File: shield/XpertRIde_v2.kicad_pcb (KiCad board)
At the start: 2 copper layers, 55.3 x 50.5 mm, 44 parts, among them J1 Conn_01x20, J2 USB_B_Micro, J3 Conn_02x05_Counter_Clockwise, J4 Conn_01x01_Female, J5 Conn_01x01_Female, J6 Conn_01x01_Female, J7 Conn_01x05, SW1 SW_DPDT_x2, U1 MCP6N11-001, U2 ADG728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

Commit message: new design
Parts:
- J7: value Conn_01x05 -> Conn_02x10_Odd_Even; footprint Connector_FFC-FPC:TE_84952-5_1x05-1MP_P1.0mm_Horizontal -> Pin_Headers:Pin_Header_Straight_2x10_Pitch2.54mm
- moved J7 34.4 mm to (68.9, 103.0), turned to 270 degrees
- moved R18 12.4 mm to (71.9, 82.3)
- moved U5 12.4 mm to (78.0, 75.6)
- moved C1 12.4 mm to (64.8, 80.7)
- moved C2 12.4 mm to (59.8, 93.7)
- moved C4 12.4 mm to (77.8, 80.6)
- moved C5 12.4 mm to (81.0, 75.6)
- moved R1 12.4 mm to (58.2, 81.4)
- moved R10 12.4 mm to (84.1, 94.2)
- moved R11 12.4 mm to (84.1, 92.7)
- moved R12 12.4 mm to (84.1, 91.2)
- moved R13 12.4 mm to (81.1, 80.6)
- moved R14 12.4 mm to (84.4, 86.4)
- moved R16 12.4 mm to (84.4, 83.6)
- moved R17 12.4 mm to (84.4, 82.2)
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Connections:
- J7 pad 1: /AMP_OUT -> /TWI_CLK
- J7 pad 2: /TWI_CLK -> /TWI_SDA
- J7 pad 3: /TWI_SDA -> /AMP_OUT
- J7 pad 4: VDD -> (no net)
- J7 pad 5: GNDD -> (no net)
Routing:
- net VDD: track 186.7 -> 149.1 mm, vias 15 -> 12
- net /AMP_OUT: track 70.2 -> 42.4 mm, vias 5 -> 4
- net /Sensor8: track 10.6 -> 28.2 mm
- net /Sensor7: track 12.1 -> 28.7 mm
- net /Sensor6: track 13.9 -> 29.2 mm
- net /Sensor3: track 13.9 -> 27.8 mm
- net /Sensor5: track 16.3 -> 29.8 mm
- net /Sensor2: track 12.7 -> 25.3 mm
- net /Sensor1: track 13.2 -> 25.7 mm
- net /Sensor4: track 14.5 -> 26.8 mm
- net GNDD: track 67.4 -> 56.7 mm, vias 32 -> 47
- net /TWI_SDA: track 81.6 -> 90.8 mm, vias 5 -> 7
- net /TWI_CLK: track 86.9 -> 80.6 mm, vias 6 -> 3
- net Net-(R5-Pad1): track 9.64 -> 11.8 mm

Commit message: MOdif_size
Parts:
- moved G*** 3.83 mm to (62.6, 69.1)
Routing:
- net Net-(J6-Pad1): vias 0 -> 2
- net VDD: vias 12 -> 13
- net GNDD: vias 47 -> 99
- net /TWI_CLK: vias 3 -> 4
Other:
- board size 55.3 x 50.5 mm -> 59.6 x 59.6 mm

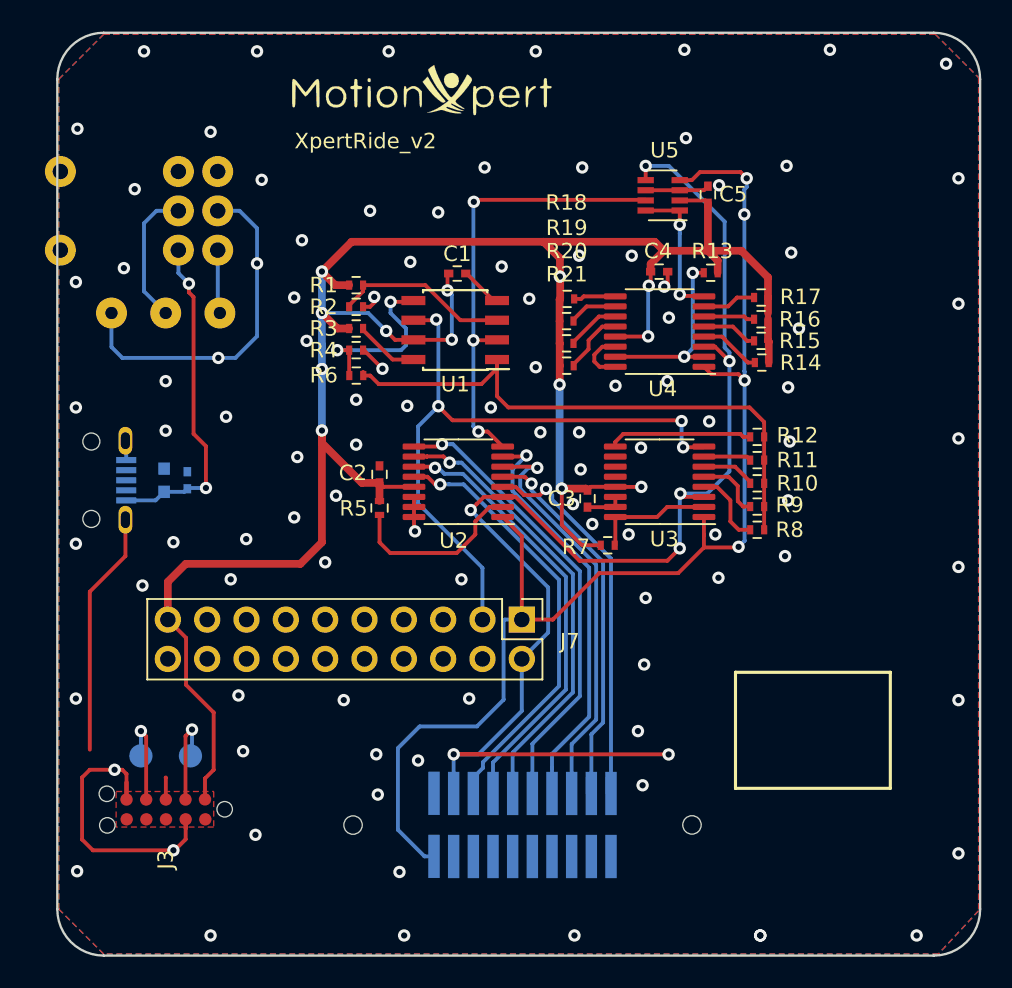
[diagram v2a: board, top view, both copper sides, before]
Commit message: new PCB dimensions
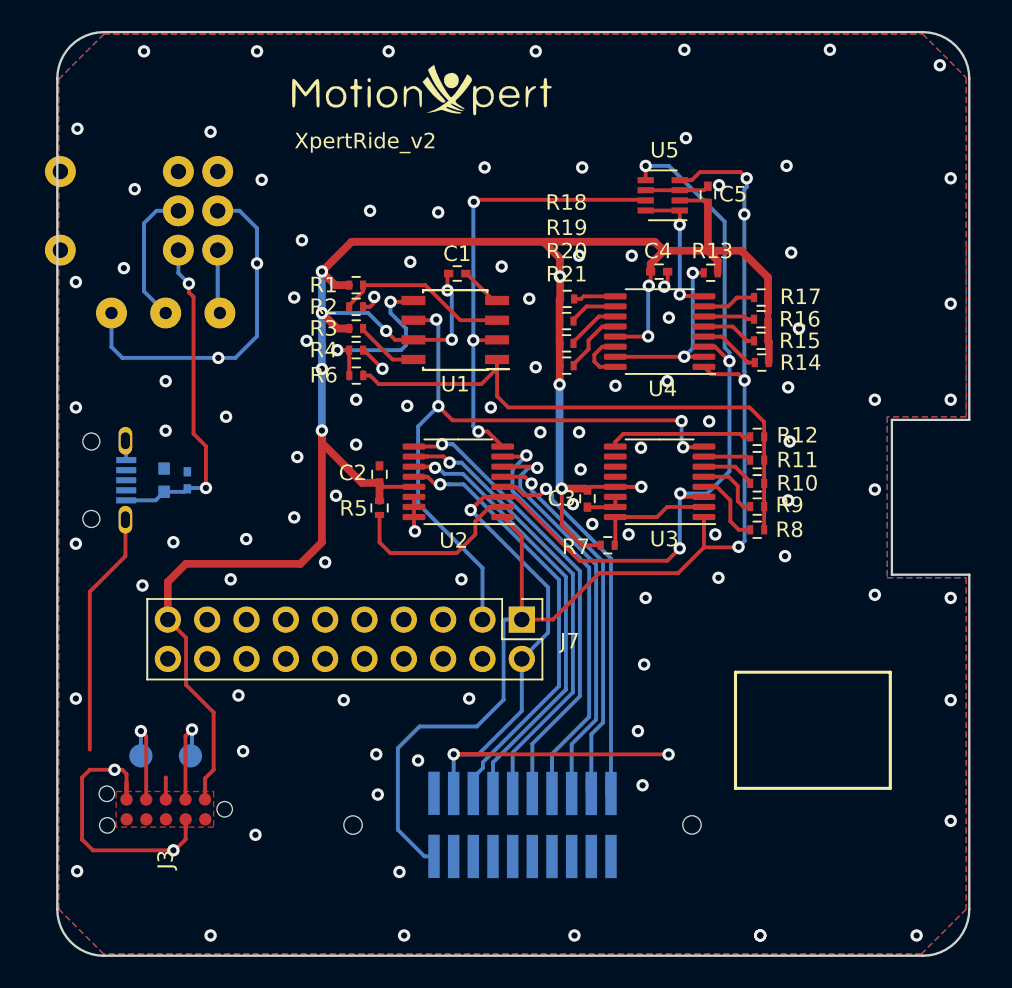
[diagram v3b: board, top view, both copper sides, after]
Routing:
- net GNDD: vias 99 -> 102
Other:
- board size 59.6 x 59.6 mm -> 58.9 x 59.7 mm
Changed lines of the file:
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@@
   (general
     (thickness 1.6)
-    (drawings 13)
-    (tracks 604)
+    (drawings 17)
+    (tracks 607)
     (zones 0)
     (modules 44)
@@
     (mod_text_size 1 1)
     (mod_text_width 0.15)
-    (pad_size 1.524 1.524)
-    (pad_drill 0.762)
+    (pad_size 2 2)
+    (pad_drill 1)
     (pad_to_mask_clearance 0.051)
     (solder_mask_min_width 0.25)
@@
     (fp_line (start 4 0) (end -4 0) (layer B.SilkS) (width 0.15))
     (fp_line (start -4 7.6) (end 4 7.6) (layer B.SilkS) (width 0.15))
-    (pad "" thru_hole circle (at 2.54 0 90) (size 2 2) (drill 1) (layers *.Cu *.Mask))
-    (pad "" thru_hole circle (at -2.54 0 90) (size 2 2) (drill 1) (layers *.Cu *.Mask))
+    (pad "" np_thru_hole circle (at 2.54 0 90) (size 2 2) (drill 1) (layers *.Cu *.Mask))
+    (pad "" np_thru_hole circle (at -2.54 0 90) (size 2 2) (drill 1) (layers *.Cu *.Mask))
     (pad 6 thru_hole circle (at -2.54 10.16 90) (size 2 2) (drill 1) (layers *.Cu *.Mask)
       (net 16 "Net-(J4-Pad1)"))
@@
     )
   )
-  (gr_arc (start 41.94 121.74) (end 38.94 121.74) (angle -90) (layer Edge.Cuts) (width 0.15))
-  (gr_arc (start 95.54 121.74) (end 95.54 124.74) (angle -90) (layer Edge.Cuts) (width 0.15))
-  (gr_arc (start 95.54 68.14) (end 98.54 68.14) (angle -90) (layer Edge.Cuts) (width 0.15))
-  (gr_arc (start 41.94 68.14) (end 41.94 65.14) (angle -90) (layer Edge.Cuts) (width 0.15))
-  (gr_line (start 98.54 68.14) (end 98.54 121.74) (layer Edge.Cuts) (width 0.15))
-  (gr_line (start 38.94 121.74) (end 38.94 68.14) (layer Edge.Cuts) (width 0.15))
-  (gr_line (start 95.54 124.74) (end 41.94 124.74) (layer Edge.Cuts) (width 0.15))
-  (gr_line (start 41.94 65.14) (end 95.54 65.14) (layer Edge.Cuts) (width 0.15))
+  (gr_line (start 97.84 100.14) (end 97.84 121.75) (layer Edge.Cuts) (width 0.15))
+  (gr_line (start 97.84 68.1) (end 97.84 90.14) (layer Edge.Cuts) (width 0.15))
+  (gr_line (start 92.84 100.14) (end 97.84 100.14) (layer Edge.Cuts) (width 0.15))
+  (gr_line (start 92.84 90.14) (end 92.84 100.14) (layer Edge.Cuts) (width 0.15))
+  (gr_line (start 97.84 90.14) (end 92.84 90.14) (layer Edge.Cuts) (width 0.15))
+  (gr_arc (start 41.94 121.75) (end 38.94 121.75) (angle -90) (layer Edge.Cuts) (width 0.15))
+  (gr_arc (start 94.84 121.75) (end 94.84 124.75) (angle -90) (layer Edge.Cuts) (width 0.15))
+  (gr_arc (start 94.84 68.1) (end 97.84 68.1) (angle -90) (layer Edge.Cuts) (width 0.15))
+  (gr_arc (start 41.94 68.1) (end 41.94 65.1) (angle -90) (layer Edge.Cuts) (width 0.15))
+  (gr_line (start 38.94 121.75) (end 38.94 68.1) (layer Edge.Cuts) (width 0.15))
+  (gr_line (start 94.84 124.75) (end 41.94 124.75) (layer Edge.Cuts) (width 0.15))
+  (gr_line (start 41.94 65.1) (end 94.84 65.1) (layer Edge.Cuts) (width 0.15))
   (gr_text XpertRide_v2 (at 58.84 72.14) (layer F.SilkS)
     (effects (font (size 1 1) (thickness 0.15)))
@@
   (via (at 78.44 83.54) (size 0.8) (drill 0.4) (layers F.Cu B.Cu) (net 2))
   (via (at 88.84 66.24) (size 0.8) (drill 0.4) (layers F.Cu B.Cu) (net 2))
-  (via (at 96.34 67.14) (size 0.8) (drill 0.4) (layers F.Cu B.Cu) (net 2))
-  (via (at 97.14 74.54) (size 0.8) (drill 0.4) (layers F.Cu B.Cu) (net 2))
-  (via (at 97.14 82.64) (size 0.8) (drill 0.4) (layers F.Cu B.Cu) (net 2))
-  (via (at 97.14 91.34) (size 0.8) (drill 0.4) (layers F.Cu B.Cu) (net 2))
-  (via (at 97.14 99.64) (size 0.8) (drill 0.4) (layers F.Cu B.Cu) (net 2))
-  (via (at 97.14 108.24) (size 0.8) (drill 0.4) (layers F.Cu B.Cu) (net 2))
-  (via (at 97.14 118.14) (size 0.8) (drill 0.4) (layers F.Cu B.Cu) (net 2))
+  (via (at 95.94 67.24) (size 0.8) (drill 0.4) (layers F.Cu B.Cu) (net 2))
+  (via (at 96.64 74.54) (size 0.8) (drill 0.4) (layers F.Cu B.Cu) (net 2))
+  (via (at 96.64 82.64) (size 0.8) (drill 0.4) (layers F.Cu B.Cu) (net 2))
+  (via (at 96.64 108.24) (size 0.8) (drill 0.4) (layers F.Cu B.Cu) (net 2))
+  (via (at 96.64 116.04) (size 0.8) (drill 0.4) (layers F.Cu B.Cu) (net 2))
   (via (at 94.44 123.44) (size 0.8) (drill 0.4) (layers F.Cu B.Cu) (net 2))
   (via (at 84.34 123.44) (size 0.8) (drill 0.4) (layers F.Cu B.Cu) (net 2))
@@
   (via (at 59.64 114.34) (size 0.8) (drill 0.4) (layers F.Cu B.Cu) (net 2))
   (via (at 61.04 119.34) (size 0.8) (drill 0.4) (layers F.Cu B.Cu) (net 2))
+  (via (at 96.64 88.84) (size 0.8) (drill 0.4) (layers F.Cu B.Cu) (net 2))
+  (via (at 91.74 88.84) (size 0.8) (drill 0.4) (layers F.Cu B.Cu) (net 2))
+  (via (at 91.74 94.64) (size 0.8) (drill 0.4) (layers F.Cu B.Cu) (net 2))
+  (via (at 91.74 101.44) (size 0.8) (drill 0.4) (layers F.Cu B.Cu) (net 2))
+  (via (at 96.64 101.64) (size 0.8) (drill 0.4) (layers F.Cu B.Cu) (net 2))
   (segment (start 47.14 94.79) (end 47.34 94.59) (width 0.25) (layer B.Cu) (net 3) (status 30))
   (segment (start 45.84 94.79) (end 47.14 94.79) (width 0.25) (layer B.Cu) (net 3) (status 30))
@@
     (polygon
       (pts
-        (xy 39.04 68.14) (xy 41.94 65.24) (xy 95.64 65.24) (xy 98.44 68.04) (xy 98.44 121.84)
-        (xy 95.84 124.64) (xy 41.94 124.64) (xy 39.04 121.74)
+        (xy 39.04 68.14) (xy 41.94 65.24) (xy 94.84 65.24) (xy 97.64 68.04) (xy 97.64 89.94)
+        (xy 92.54 89.94) (xy 92.54 100.34) (xy 97.64 100.34) (xy 97.64 121.74) (xy 94.74 124.64)
+        (xy 41.94 124.64) (xy 39.04 121.74)
       )
     )
@@
     (polygon
       (pts
-        (xy 39.04 68.14) (xy 41.94 65.24) (xy 95.64 65.24) (xy 98.44 68.04) (xy 98.44 121.84)
-        (xy 95.84 124.64) (xy 41.94 124.64) (xy 39.04 121.74)
+        (xy 39.04 68.14) (xy 41.94 65.24) (xy 94.84 65.24) (xy 97.64 68.04) (xy 97.64 78.99)
+        (xy 97.64 89.94) (xy 92.54 89.94) (xy 92.54 100.34) (xy 97.64 100.34) (xy 97.64 121.74)
+        (xy 94.74 124.64) (xy 41.94 124.64) (xy 39.04 121.74)
       )
     )

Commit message: modif dimensions-joint
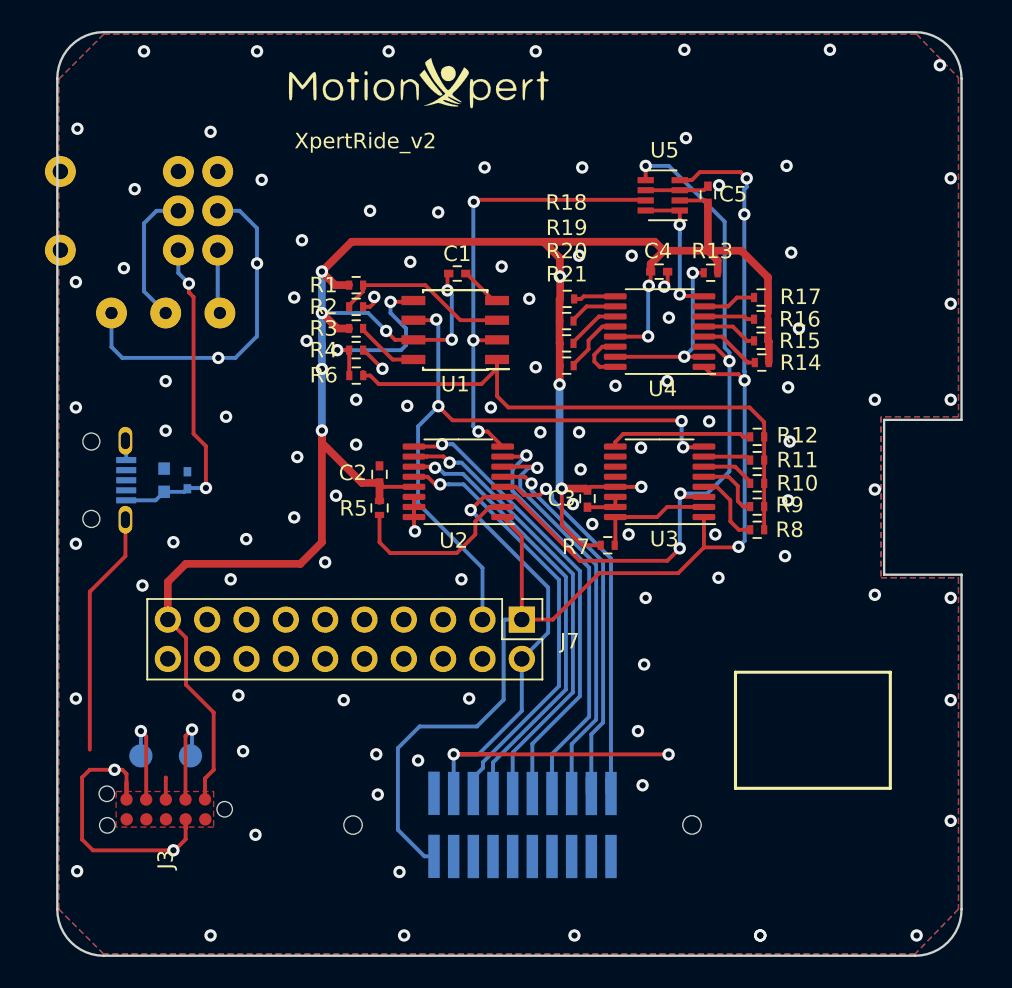
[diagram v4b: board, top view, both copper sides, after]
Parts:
- moved G*** 0.49 mm to (62.4, 68.7)
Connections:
- J2 pad 2: (no net) -> Net-(J2-Pad2)
- J2 pad 3: (no net) -> Net-(J2-Pad3)
- J2 pad 4: (no net) -> Net-(J2-Pad4)
- J3 pad 10: (no net) -> Net-(J3-Pad10)
- J3 pad 6: (no net) -> Net-(J3-Pad6)
- J3 pad 7: (no net) -> Net-(J3-Pad7)
- J3 pad 8: (no net) -> Net-(J3-Pad8)
- J7 pad 10: (no net) -> Net-(J7-Pad10)
- J7 pad 11: (no net) -> Net-(J7-Pad11)
- J7 pad 12: (no net) -> Net-(J7-Pad12)
- J7 pad 13: (no net) -> Net-(J7-Pad13)
- J7 pad 14: (no net) -> Net-(J7-Pad14)
- J7 pad 15: (no net) -> Net-(J7-Pad15)
- J7 pad 16: (no net) -> Net-(J7-Pad16)
- J7 pad 17: (no net) -> Net-(J7-Pad17)
- J7 pad 18: (no net) -> Net-(J7-Pad18)
- J7 pad 4: (no net) -> Net-(J7-Pad4)
- J7 pad 5: (no net) -> Net-(J7-Pad5)
- J7 pad 6: (no net) -> Net-(J7-Pad6)
- J7 pad 7: (no net) -> Net-(J7-Pad7)
- J7 pad 8: (no net) -> Net-(J7-Pad8)
- J7 pad 9: (no net) -> Net-(J7-Pad9)
- SW1 pad 1: (no net) -> Net-(SW1-Pad1)
- SW1 pad 4: (no net) -> Net-(SW1-Pad4)
- U3 pad 10: (no net) -> Net-(U3-Pad10)
- U3 pad 11: (no net) -> Net-(U3-Pad11)
- U3 pad 12: (no net) -> Net-(U3-Pad12)
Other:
- board size 58.9 x 59.7 mm -> 58.4 x 59.7 mm

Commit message: fixed switch position
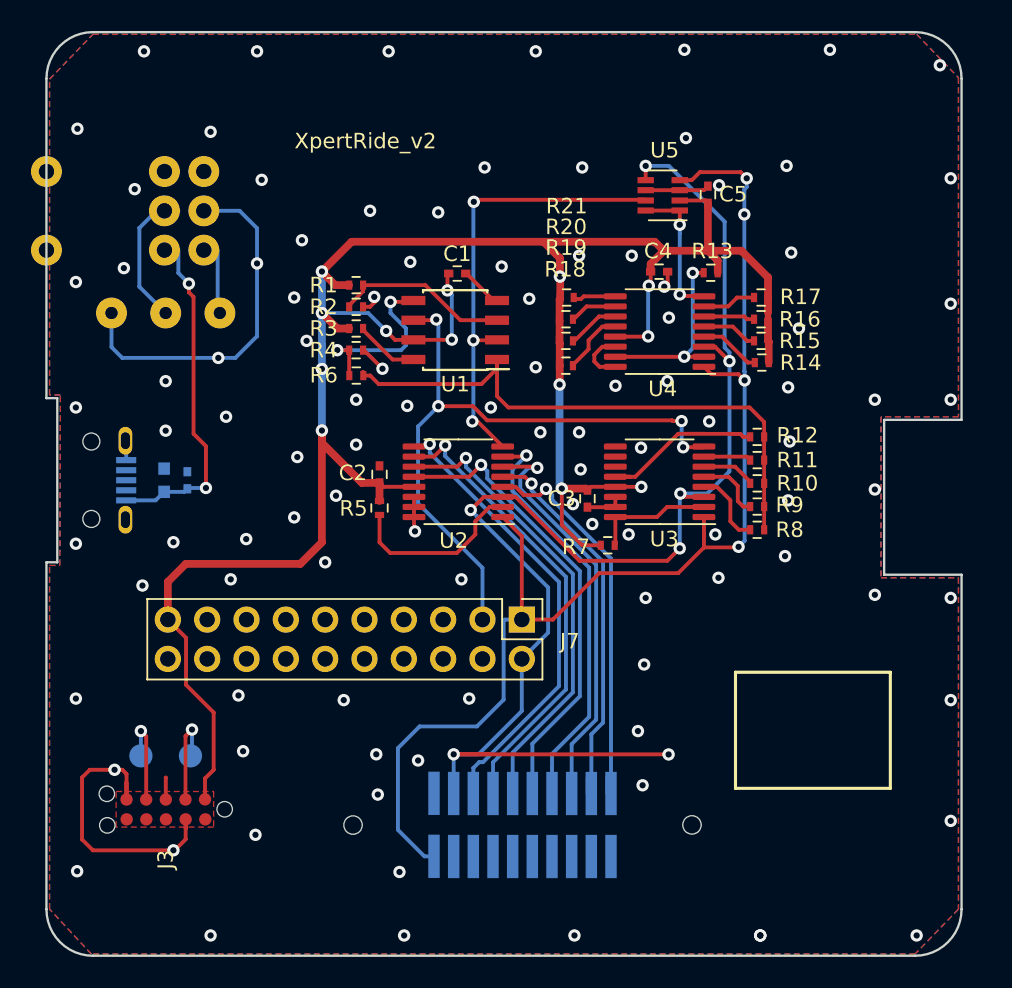
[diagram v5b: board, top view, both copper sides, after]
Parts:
- removed G***: LOGO, Logos:vector_lab_negatif_19_5mm
- moved R21 4.40 mm to (71.8, 82.2)
- moved R18 4.31 mm to (71.8, 86.6)
- moved R20 1.56 mm to (71.8, 83.6)
- moved R19 1.28 mm to (71.8, 85.0)
- moved SW1 0.90 mm to (38.2, 76.6)
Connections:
- U2 pad 10: /Sensor6 -> /Sensor7
- U2 pad 11: /Sensor7 -> /Sensor6
- U2 pad 12: /Sensor8 -> /Sensor5
- U2 pad 9: /Sensor5 -> /Sensor8
- U3 pad 12: Net-(U3-Pad12) -> Net-(R12-Pad1)
- U3 pad 9: Net-(R12-Pad1) -> Net-(U3-Pad9)
- U4 pad 10: Net-(R19-Pad1) -> Net-(R20-Pad1)
- U4 pad 11: Net-(R20-Pad1) -> Net-(R19-Pad1)
- U4 pad 12: Net-(R21-Pad1) -> Net-(R18-Pad1)
- U4 pad 9: Net-(R18-Pad1) -> Net-(R21-Pad1)
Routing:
- net GNDD: track 56.7 -> 40.9 mm
- net Net-(R12-Pad1): track 9.31 -> 10.9 mm
- net Net-(R21-Pad1): track 4.13 -> 2.73 mm
- net Net-(R18-Pad1): track 2.73 -> 4.13 mm
- net /Sensor8: track 28.2 -> 29.5 mm
- net /Sensor7: track 28.7 -> 30.0 mm
- net /Sensor6: track 29.2 -> 29.7 mm
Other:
- board size 58.4 x 59.7 mm -> 59.1 x 59.7 mm
